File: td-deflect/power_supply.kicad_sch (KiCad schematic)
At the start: 68 parts, among them J13 Conn_01x02_Male, J14 Conn_01x02_Male, J15 Conn_01x02_Male, J18 Conn_01x02_Male, J2 Conn_01x02_Male, J8 Conn_01x02_Male, J9 Conn_01x02_Male, Q12 C2M0045170D, Q13 BSC082N10LSG, U13 MCP1416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

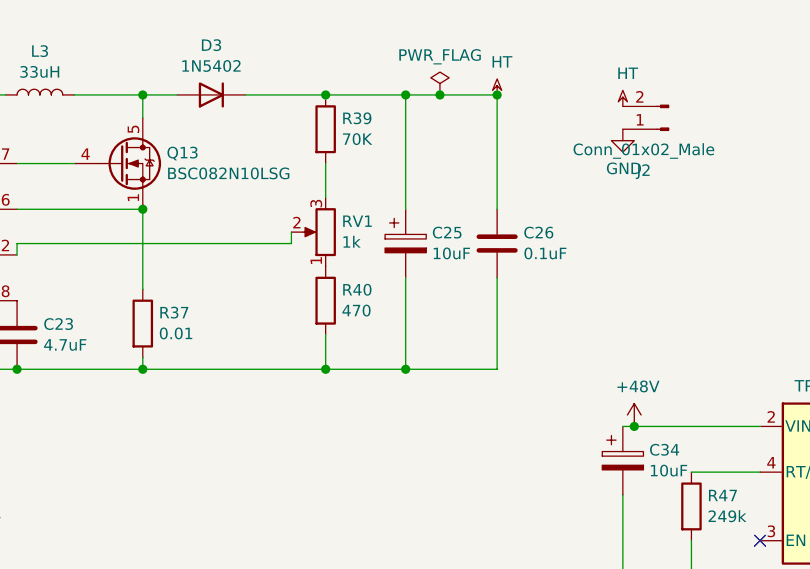
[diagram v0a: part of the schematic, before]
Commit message: update some transistors, remove current sense amp
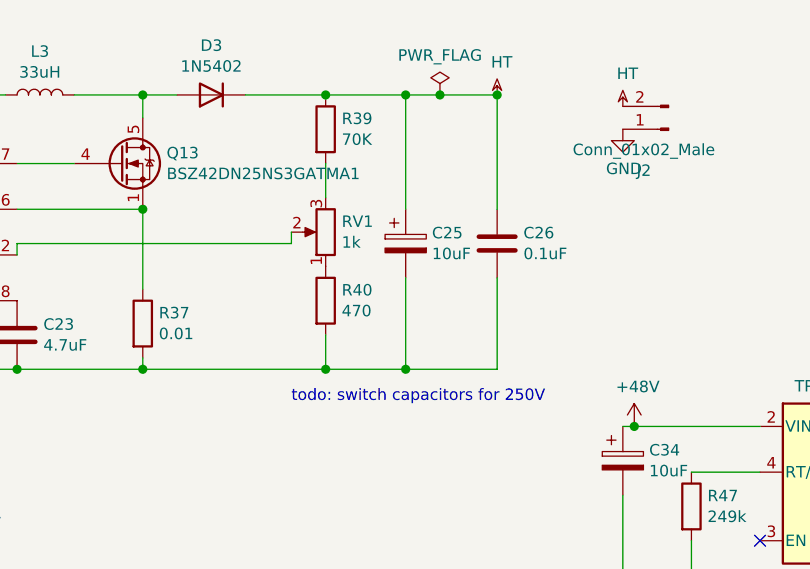
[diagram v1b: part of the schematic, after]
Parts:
- C25, C26: Voltage 200V -> 250V
- Q13: value BSC082N10LSG -> BSZ42DN25NS3GATMA1; Digikey BSC082N10LSGATMA1CT-ND -> BSZ42DN25NS3GATMA1CT-ND
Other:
- note added: "todo: switch capacitors for 250V"
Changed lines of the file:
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@@
+    (effects (font (size 1.27 1.27)) (justify left bottom))
+  )
+  (text "todo: switch capacitors for 250V" (at 120.65 63.5 0)
     (effects (font (size 1.27 1.27)) (justify left bottom))
   )
@@
       (effects (font (size 1.27 1.27)) (justify left))
     )
-    (property "Value" "BSC082N10LSG" (id 1) (at 106.7816 37.973 0)
+    (property "Value" "BSZ42DN25NS3GATMA1" (id 1) (at 106.7816 37.973 0)
       (effects (font (size 1.27 1.27)) (justify left))
     )
@@
       (effects (font (size 1.27 1.27) italic) (justify left) hide)
     )
-    (property "Datasheet" "http://www.infineon.com/dgdl/Infineon-BSC082N10LS-DS-v01_07-en.pdf?fileId=db3a3043163797a6011647faad240719" (id 3) (at 101.6 36.83 90)
+    (property "Datasheet" "" (id 3) (at 101.6 36.83 90)
       (effects (font (size 1.27 1.27)) (justify left) hide)
     )
-    (property "Digikey" "BSC082N10LSGATMA1CT-ND" (id 4) (at 101.6 36.83 0)
+    (property "Digikey" "BSZ42DN25NS3GATMA1CT-ND" (id 4) (at 101.6 36.83 0)
       (effects (font (size 1.27 1.27)) hide)
     )
@@
       (effects (font (size 1.27 1.27)) hide)
     )
-    (property "Voltage" "200V" (id 4) (at 133.35 45.72 0)
+    (property "Voltage" "250V" (id 4) (at 133.35 45.72 0)
       (effects (font (size 1.27 1.27)) hide)
     )
@@
       (effects (font (size 1.27 1.27)) hide)
     )
-    (property "Voltage" "200V" (id 4) (at 143.51 45.72 0)
-      (effects (font (size 1.27 1.27)) hide)
-    )
+    (property "Voltage" "250V" (id 4) (at 143.51 45.72 0)
+      (effects (font (size 1.27 1.27)) hide)
+    )

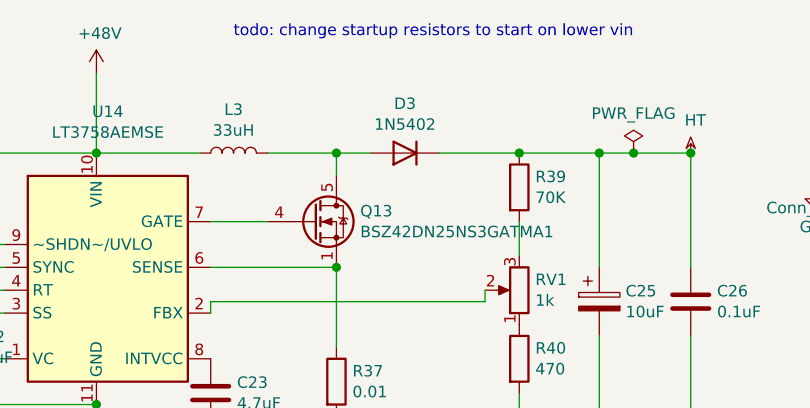
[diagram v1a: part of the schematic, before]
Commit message: switch b+ diode to sic
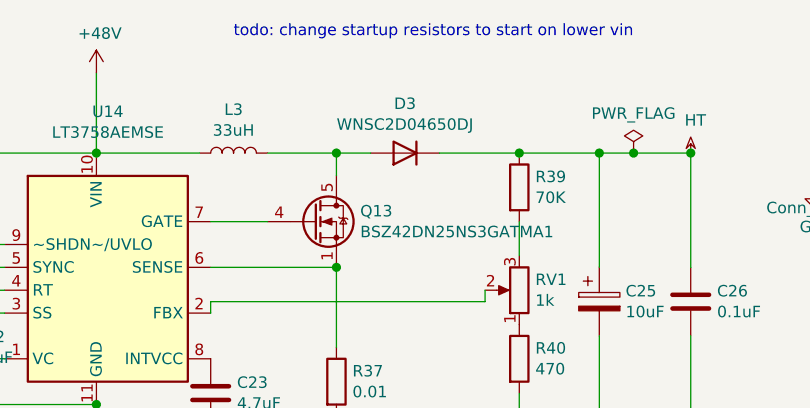
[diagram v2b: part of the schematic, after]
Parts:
- D3: value 1N5402 -> WNSC2D04650DJ; footprint Diode_THT:D_DO-201AD_P15.24mm_Horizontal -> Package_TO_SOT_SMD:TO-252-2_TabPin1; Digikey 1N5402GOS-ND -> 1740-WNSC2D04650DJCT-ND
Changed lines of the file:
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@@
     (in_bom yes) (on_board yes)
     (property "Reference" "D3" (id 0) (at 111.76 23.7236 0))
-    (property "Value" "1N5402" (id 1) (at 111.76 26.035 0))
-    (property "Footprint" "Diode_THT:D_DO-201AD_P15.24mm_Horizontal" (id 2) (at 111.76 24.765 0)
+    (property "Value" "WNSC2D04650DJ" (id 1) (at 111.76 26.035 0))
+    (property "Footprint" "Package_TO_SOT_SMD:TO-252-2_TabPin1" (id 2) (at 111.76 24.765 0)
       (effects (font (size 1.27 1.27)) hide)
     )
-    (property "Datasheet" "http://www.vishay.com/docs/88516/1n5400.pdf" (id 3) (at 111.76 29.21 0)
+    (property "Datasheet" "" (id 3) (at 111.76 29.21 0)
       (effects (font (size 1.27 1.27)) hide)
     )
-    (property "Digikey" "1N5402GOS-ND " (id 4) (at 111.76 29.21 0)
+    (property "Digikey" "1740-WNSC2D04650DJCT-ND" (id 4) (at 111.76 29.21 0)
       (effects (font (size 1.27 1.27)) hide)
     )

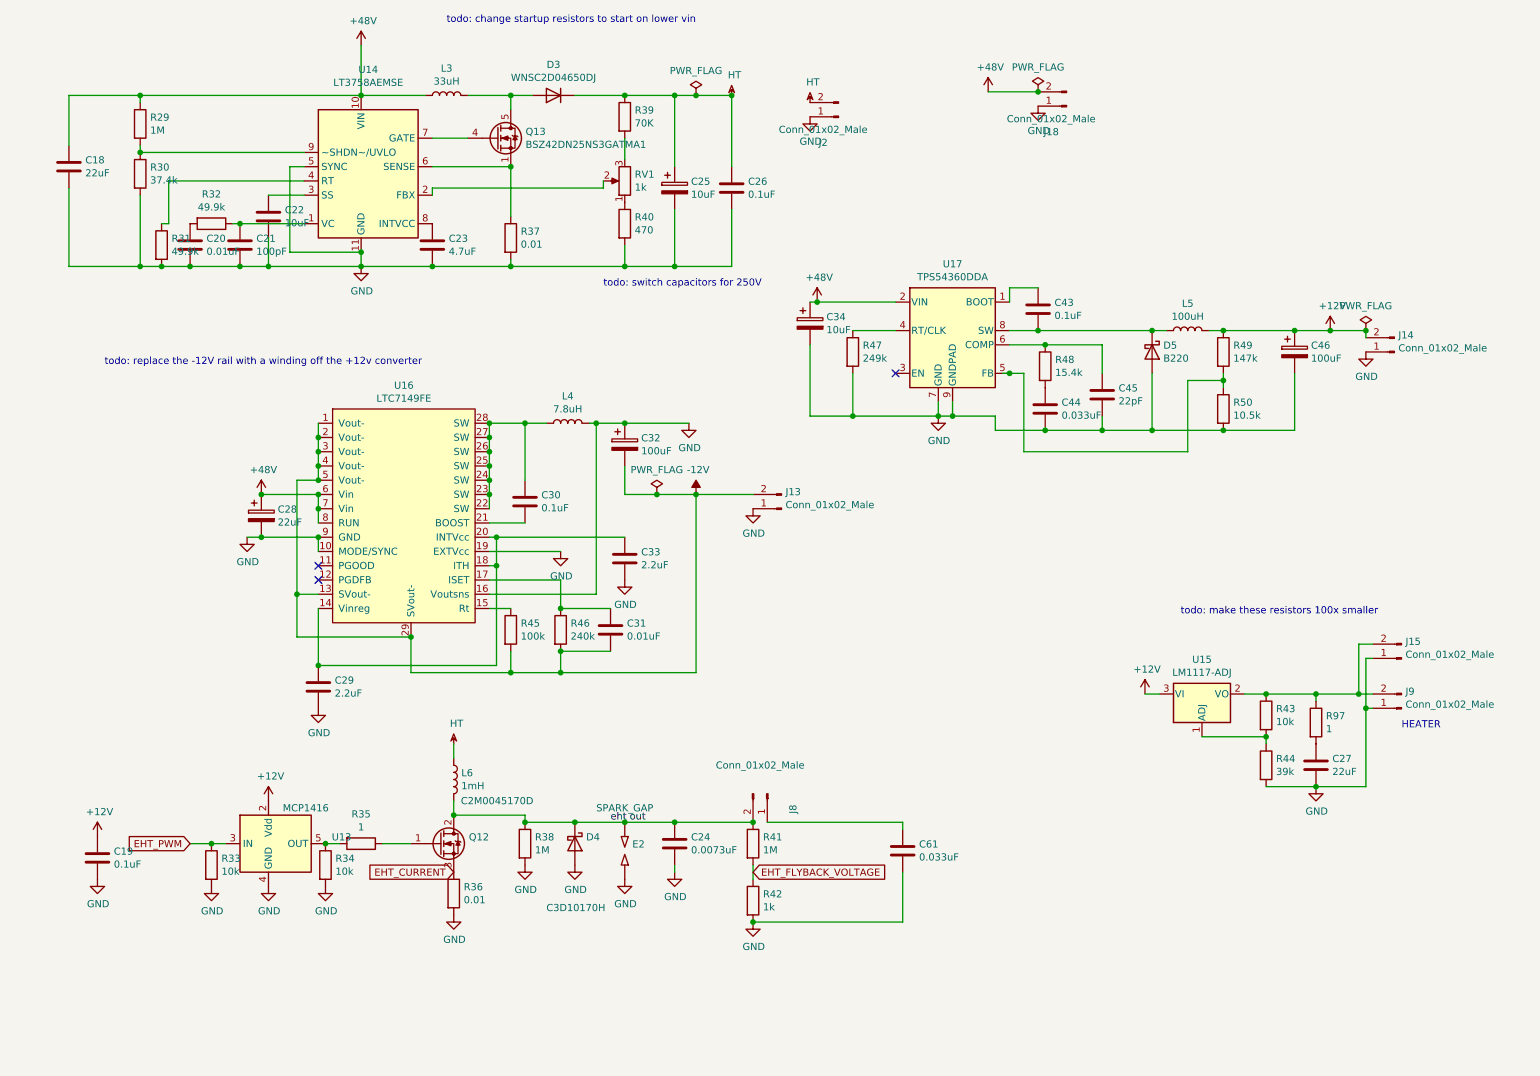
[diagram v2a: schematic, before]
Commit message: switch ti to rohm switching power ic
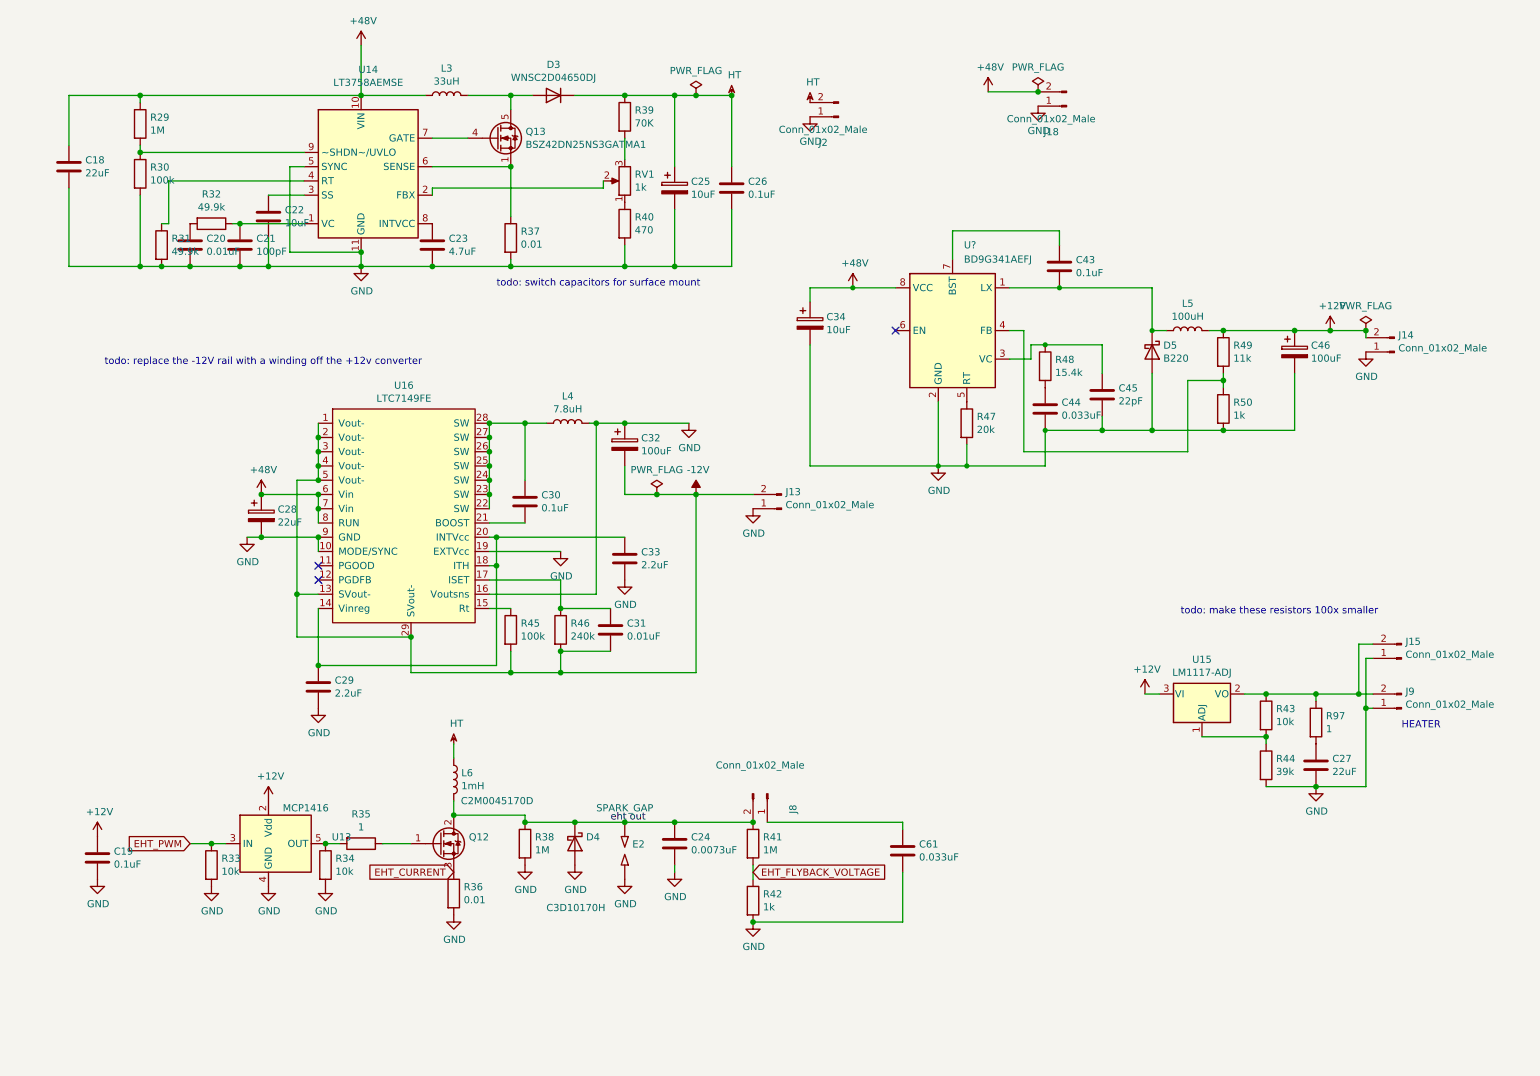
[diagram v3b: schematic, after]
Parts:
- removed U17: TPS54360DDA, Package_SO:TI_SO-PowerPAD-8_ThermalVias, symbol Regulator_Switching:TPS54360DDA
- added U?: BD9G341AEFJ, Package_SO:SOIC-8-1EP_3.9x4.9mm_P1.27mm_EP2.41x3.3mm_ThermalVias, symbol Regulator_Switching:BD9G341EFJ
- R30: value 37.4k -> 100k; Digikey 311-37.4KCRCT-ND -> (none)
- R47: value 249k -> 20k; Digikey 311-249KCRCT-ND -> (none)
- R49: value 147k -> 11k; Digikey 311-147KCRCT-ND -> (none)
- R50: value 10.5k -> 1k; Digikey 311-10.5KCRCT-ND -> (none)
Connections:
- net +48V: now also U?.8 (VCC)
- net GND: now also U?.2 (GND)
- net at C43.1: now also U?.7 (BST)
- net at R47.1: now also U?.5 (RT)
- net at R49.2, R50.1: now also U?.4 (FB)
- net at C45.1, R48.1: now also U?.3 (VC)
- net at C43.2, D5.1 (K), L5.1: now also U?.1 (LX)
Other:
- note added: "todo: switch capacitors for surface mount"
- note removed: "todo: change startup resistors to start on lower vin"
- note removed: "todo: switch capacitors for 250V"
- moved on the sheet: C43, R47

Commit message: replace negative supply with coupled inductor
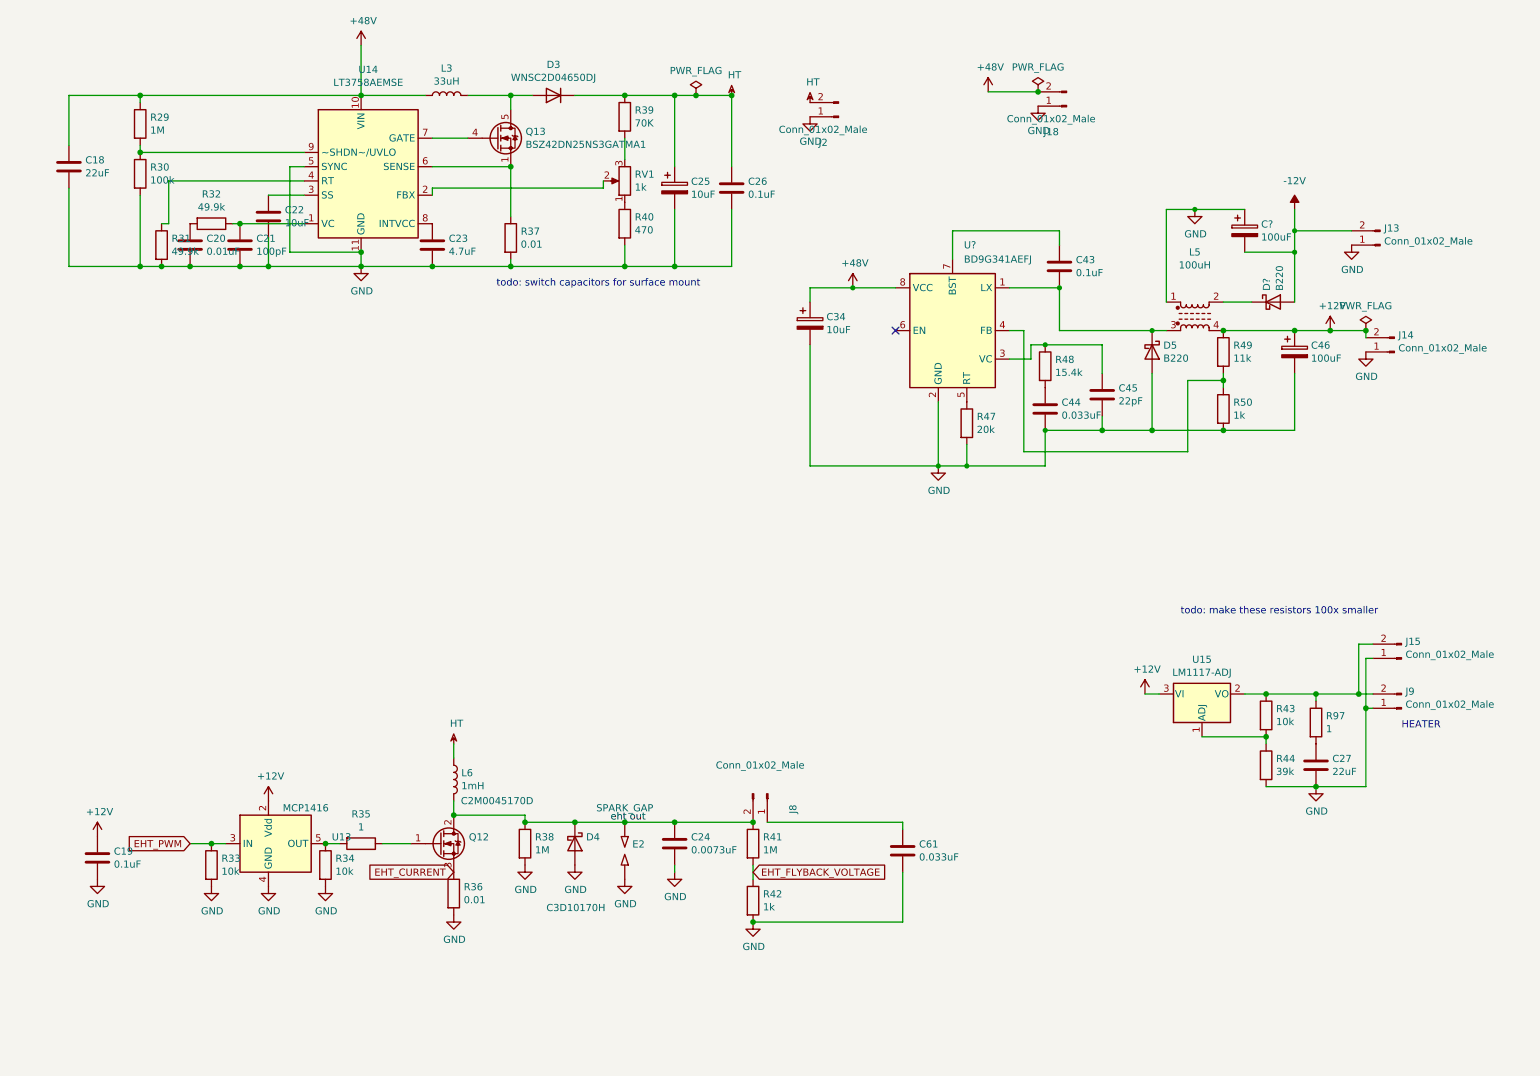
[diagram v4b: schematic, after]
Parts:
- removed C28: 22uF, Capacitor_THT:CP_Radial_D8.0mm_P3.50mm, symbol Device:CP
- removed C29, C33: 2.2uF, Capacitor_SMD:C_0805_2012Metric_Pad1.15x1.40mm_HandSolder, symbol Device:C
- removed C30: 0.1uF, Capacitor_SMD:C_0805_2012Metric_Pad1.15x1.40mm_HandSolder, symbol Device:C
- removed C31: 0.01uF, Capacitor_SMD:C_0805_2012Metric_Pad1.15x1.40mm_HandSolder, symbol Device:C
- removed C32: 100uF, Capacitor_THT:CP_Radial_D8.0mm_P3.50mm, symbol Device:CP
- removed L4: 7.8uH, Inductor_SMD:L_Bourns_SRR1260, symbol Device:L
- removed R45: 100k, Resistor_SMD:R_0805_2012Metric_Pad1.15x1.40mm_HandSolder, symbol Device:R
- removed R46: 240k, Resistor_SMD:R_0805_2012Metric_Pad1.15x1.40mm_HandSolder, symbol Device:R
- removed U16: LTC7149FE, Package_SO:HTSSOP-28-1EP_4.4x9.7mm_P0.65mm_EP2.85x5.4mm, symbol td-deflect:LTC7149FE
- added C?: 100uF, Capacitor_THT:CP_Radial_D8.0mm_P3.50mm, symbol Device:CP
- added D?: B220, Diode_SMD:D_SMB, symbol Diode:B220
- L5: footprint Inductor_SMD:L_Bourns_SRR1260 -> (none); symbol Device:L -> Device:L_Ferrite_Coupled; Digikey SRR1260-101MCT-ND -> (none)
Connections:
- net +12V: now also L5.4; no longer L5.2
- net -12V: now also C?.2, D?.2 (A)
- net GND: now also L5.1, C?.1
- net at C43.2, D5.1 (K), U?.1 (LX): now also L5.3; no longer L5.1
- new net: D?.1 (K), L5.2
- no-connect marks 3 -> 1
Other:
- note removed: "todo: replace the -12V rail with a winding off the +12v converter"
- moved on the sheet: J13
